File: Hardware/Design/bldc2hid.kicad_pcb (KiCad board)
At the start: 2 copper layers, 13 parts, among them J1 Conn_01x03_Female, J2 Conn_01x06_Female, J3 Conn_01x03_Female, J4 Conn_01x01_Female, U1 LT1492, U2 WS2811

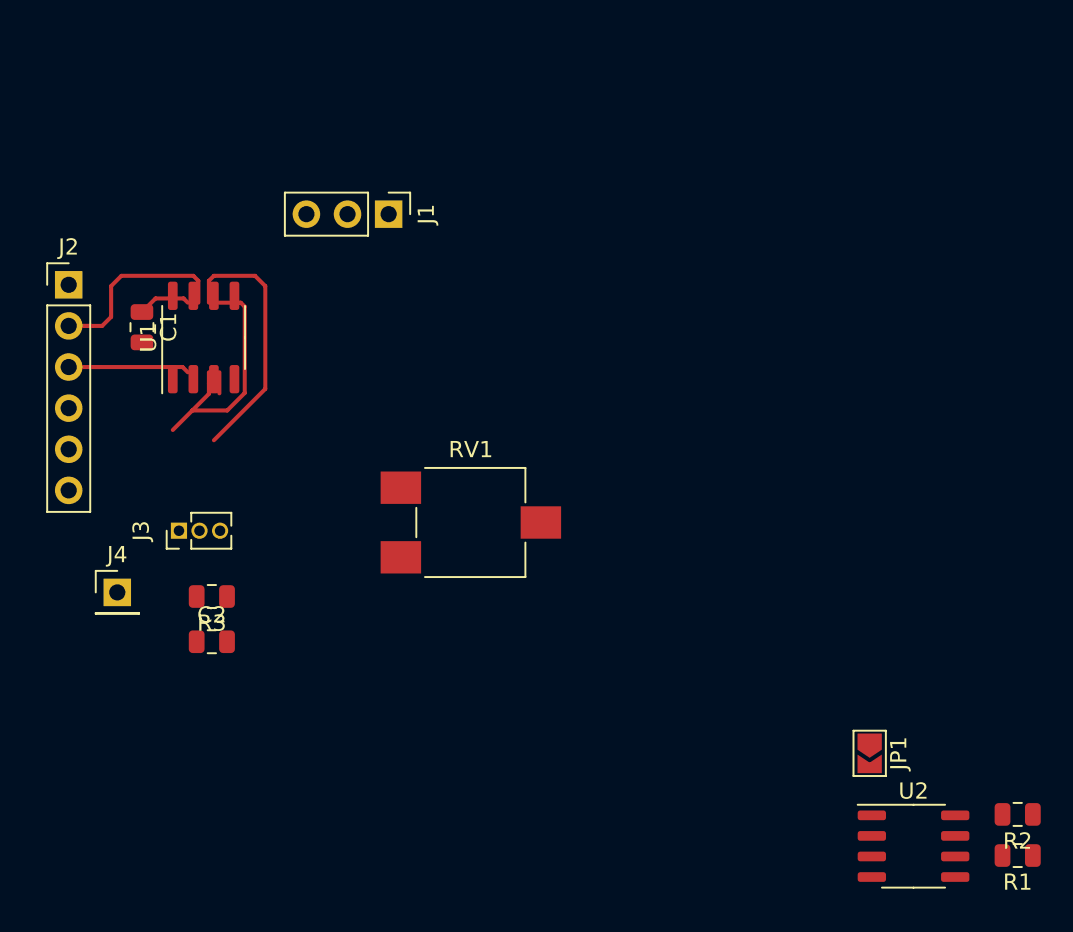
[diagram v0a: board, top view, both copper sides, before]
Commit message: Comparaison faite avec les 3 phases
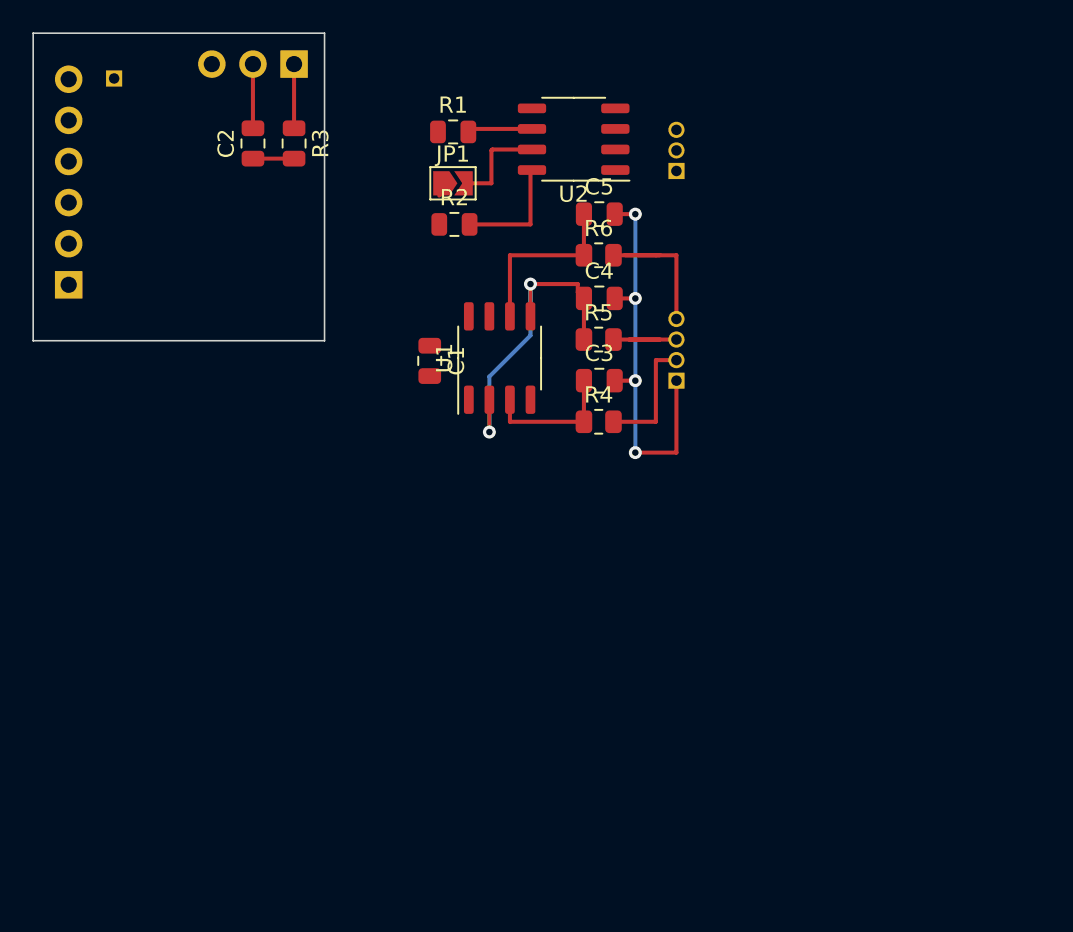
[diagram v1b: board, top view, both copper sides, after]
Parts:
- removed RV1: R_POT, Potentiometer_SMD:Potentiometer_ACP_CA6-VSMD_Vertical
- added C3: 30n, Capacitor_SMD:C_0805_2012Metric, F.Cu at (74.0, 53.5)
- added C4: 30n, Capacitor_SMD:C_0805_2012Metric, F.Cu at (74.0, 48.4)
- added C5: 30n, Capacitor_SMD:C_0805_2012Metric, F.Cu at (74.0, 43.2)
- added J5: Conn_01x03_Female, Connector_PinHeader_1.27mm:PinHeader_1x03_P1.27mm_Horizontal, B.Cu at (78.7, 40.5)
- added R4: 10K, Resistor_SMD:R_0805_2012Metric, F.Cu at (73.9, 56.0)
- added R5: 10K, Resistor_SMD:R_0805_2012Metric, F.Cu at (73.9, 50.9)
- added R6: 10K, Resistor_SMD:R_0805_2012Metric, F.Cu at (73.9, 45.7)
- J1, J2: moved to B.Cu
- J3: value Conn_01x03_Female -> Conn_01x04_Female; footprint Connector_PinHeader_1.27mm:PinHeader_1x03_P1.27mm_Vertical -> Connector_PinHeader_1.27mm:PinHeader_1x04_P1.27mm_Vertical; moved to B.Cu
- J4: footprint Connector_PinHeader_2.54mm:PinHeader_1x01_P2.54mm_Vertical -> Connector_PinHeader_1.27mm:PinHeader_1x01_P1.27mm_Horizontal; moved to B.Cu
- R3: value R -> 22M
- moved R1 56.7 mm to (64.9, 38.1), turned to 0 degrees
- moved R2 50.4 mm to (65.0, 43.8), turned to 0 degrees
- moved U2 48.5 mm to (72.4, 38.5), turned to 180 degrees
- moved JP1 43.6 mm to (64.9, 41.3), turned to 0 degrees
- moved J3 32.1 mm to (78.7, 53.5), turned to 0 degrees
- moved J4 31.8 mm to (44.0, 34.8), turned to 90 degrees
- moved C2 30.9 mm to (52.6, 38.8), turned to 90 degrees
- moved R3 28.4 mm to (55.1, 38.8), turned to 270 degrees
- moved U1 18.3 mm to (67.8, 52.1)
- moved C1 17.9 mm to (63.5, 52.2)
- moved J1 11.0 mm to (55.1, 33.9), turned to 90 degrees
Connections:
- J1 pad 3: /VIN -> (no net)
- J2 pad 4: /P3(USB+) -> (no net)
- J2 pad 5: /P4(USB-) -> (no net)
- J3 pad 1: L1 -> GND
- J3 pad 2: L2 -> L1
- J3 pad 3: GND -> L2
- U1 pad 2: /Level -> Net-(C4-Pad1)
- U1 pad 3: L1 -> Net-(C3-Pad1)
- U1 pad 5: L1 -> Net-(C4-Pad1)
- U1 pad 6: L2 -> Net-(C5-Pad1)
- U2 pad 5: Net-(U2-Pad5) -> (no net)
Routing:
- net GND: track 1.30 -> 29.5 mm, vias 0 -> 4
- net Net-(C4-Pad1): track 0.00 -> 22.7 mm, vias 0 -> 2
- net Direction: track 13.3 -> 0.00 mm
- net Net-(C5-Pad1): track 0.00 -> 10.9 mm
- net L2: track 16.1 -> 5.80 mm
- net L3: track 0.00 -> 9.99 mm
- net Net-(C3-Pad1): track 0.00 -> 8.47 mm
- net Threshold: track 8.13 -> 0.00 mm
- net L1: track 15.2 -> 7.70 mm
- net Net-(R2-Pad2): track 0.00 -> 7.16 mm
- net Net-(JP1-Pad2): track 0.00 -> 6.21 mm
- net Net-(R1-Pad2): track 0.00 -> 4.01 mm
- net CapSense: track 0.00 -> 2.54 mm
- net +5V: track 3.29 -> 4.14 mm
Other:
- board outline added: 18 x 19 mm
